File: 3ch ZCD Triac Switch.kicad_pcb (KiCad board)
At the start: 2 copper layers, 50 x 50 mm, 41 parts, among them P1 Mains_In, P2 Load_3, P3 Load_2, P4 Load_1, P5 CONN_01X06, U1 TRIAC, U2 TRIAC, U3 TRIAC, U4 TLP291, U5 TLP291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

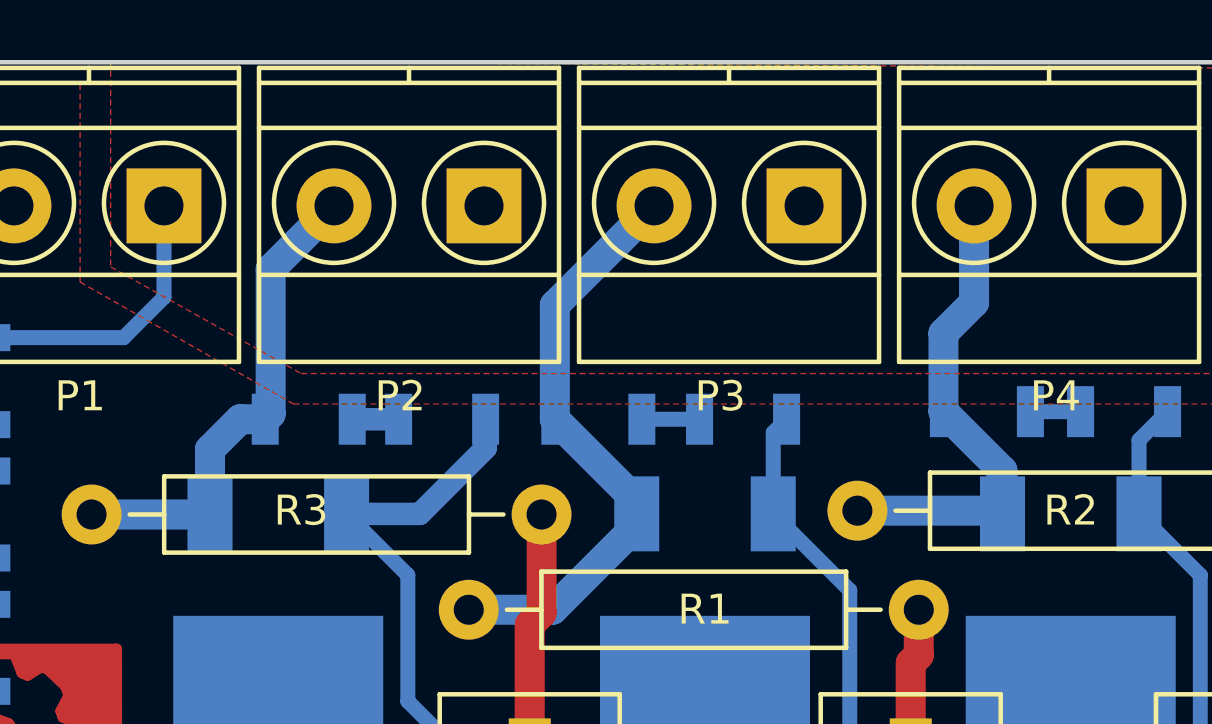
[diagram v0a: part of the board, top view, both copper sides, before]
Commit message: Triac Track Change to 2mm
2.9A with 10CdT
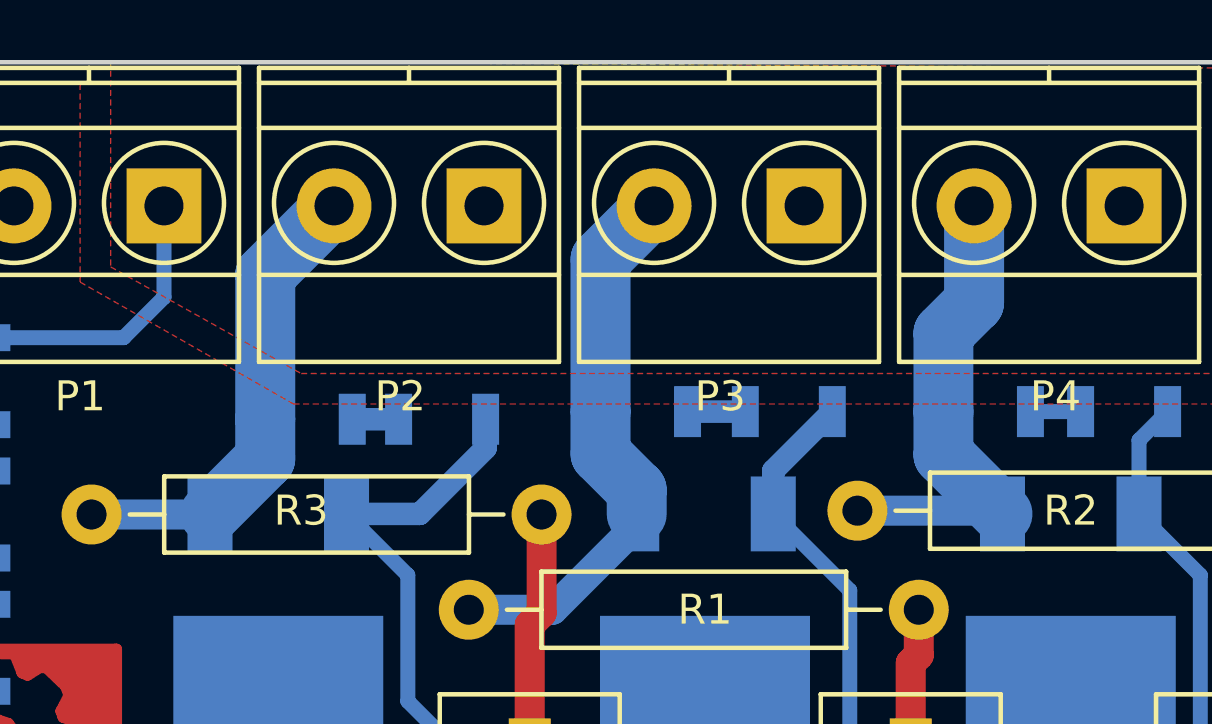
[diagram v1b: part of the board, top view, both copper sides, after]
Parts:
- moved R13 1.55 mm to (148.2, 81.6)
- moved R8 1.55 mm to (143.4, 81.6)
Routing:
- net /PH2_Out: track 20.7 -> 19.1 mm
- net /G2_Drv: track 28.3 -> 29.2 mm
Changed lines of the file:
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@@
     (links 61)
     (no_connects 0)
-    (area 116.924999 69.924999 167.075001 120.075001)
+    (area 106.479926 69.762999 167.075001 122.5)
     (thickness 1.6)
     (drawings 11)
-    (tracks 191)
+    (tracks 189)
     (zones 0)
     (modules 41)
@@
   )
   (setup
-    (last_trace_width 0.25)
+    (last_trace_width 1)
     (user_trace_width 0.25)
     (user_trace_width 0.5)
@@
     (uvia_drill 0.1)
   )
+  (module .pretty:SOT-428 (layer B.Cu)
+    (at 145.448 88.504)
+    (descr SOT428)
+    (attr smd)
+    (fp_text reference U1 (at 0 8.89 180) (layer B.SilkS)
+      (effects (font (size 1 1) (thickness 0.15)) (justify mirror))
+    )
+    (fp_text value TRIAC (at -0.09906 -0.89916) (layer B.Fab)
+      (effects (font (size 1 1) (thickness 0.15)) (justify mirror))
+    )
+    (fp_line (start -4.064 -1.016) (end 3.937 -1.016) (layer B.SilkS) (width 0.15))
+    (fp_line (start -4.064 5.588) (end -4.064 -4.445) (layer B.SilkS) (width 0.15))
+    (fp_line (start 3.937 5.588) (end 3.937 -4.445) (layer B.SilkS) (width 0.15))
+    (pad 1 smd rect (at -2.27584 -3.44932) (size 1.50114 2.49936) (layers B.Cu B.Paste B.Mask)
+      (net 7 /PH2_Out))
+    (pad 3 smd rect (at 2.27584 -3.44932) (size 1.50114 2.49936) (layers B.Cu B.Paste B.Mask)
+      (net 24 /G2_Drv))
+    (pad 2 smd rect (at 0 3.44932) (size 7.00024 7.00024) (layers B.Cu B.Paste B.Mask)
+      (net 2 /Hot_In))
+    (model TO_SOT_Packages_SMD.3dshapes/SOT-428.wrl
+      (at (xyz 0 0 0))
+      (scale (xyz 1 1 1))
+      (rotate (xyz 0 0 0))
+    )
+  )
   (module Capacitors_ThroughHole:C_Rect_L13_W6_H12_P10 (layer F.Cu)
     (at 152.306 92.568 270)
@@
   )
   (module Resistors_SMD:R_1206 (layer B.Cu)
-    (at 141.892 81.9)
+    (at 143.416 81.646)
     (descr "Resistor SMD 1206, reflow soldering, Vishay (see dcrcw.pdf)")
     (tags "resistor 1206")
@@
   )
   (module Resistors_SMD:R_1206 (layer B.Cu)
-    (at 146.718 81.9)
+    (at 148.242 81.646)
     (descr "Resistor SMD 1206, reflow soldering, Vishay (see dcrcw.pdf)")
     (tags "resistor 1206")
@@
   )
   (module .pretty:SOT-428 (layer B.Cu)
-    (at 145.448 88.504)
-    (descr SOT428)
-    (attr smd)
-    (fp_text reference U1 (at 0 8.89 180) (layer B.SilkS)
-      (effects (font (size 1 1) (thickness 0.15)) (justify mirror))
-    )
-    (fp_text value TRIAC (at -0.09906 -0.89916) (layer B.Fab)
-      (effects (font (size 1 1) (thickness 0.15)) (justify mirror))
-    )
-    (fp_line (start -4.064 -1.016) (end 3.937 -1.016) (layer B.SilkS) (width 0.15))
-    (fp_line (start -4.064 5.588) (end -4.064 -4.445) (layer B.SilkS) (width 0.15))
-    (fp_line (start 3.937 5.588) (end 3.937 -4.445) (layer B.SilkS) (width 0.15))
-    (pad 1 smd rect (at -2.27584 -3.44932) (size 1.50114 2.49936) (layers B.Cu B.Paste B.Mask)
-      (net 7 /PH2_Out))
-    (pad 3 smd rect (at 2.27584 -3.44932) (size 1.50114 2.49936) (layers B.Cu B.Paste B.Mask)
-      (net 24 /G2_Drv))
-    (pad 2 smd rect (at 0 3.44932) (size 7.00024 7.00024) (layers B.Cu B.Paste B.Mask)
-      (net 2 /Hot_In))
-    (model TO_SOT_Packages_SMD.3dshapes/SOT-428.wrl
-      (at (xyz 0 0 0))
-      (scale (xyz 1 1 1))
-      (rotate (xyz 0 0 0))
-    )
-  )
-  (module .pretty:SOT-428 (layer B.Cu)
     (at 131.224 88.504)
     (descr SOT428)
@@
   (segment (start 126.07 79.18) (end 127.414 77.836) (width 0.5) (layer B.Cu) (net 5))
   (segment (start 127.414 77.836) (end 127.414 74.788) (width 0.5) (layer B.Cu) (net 5))
-  (segment (start 128.94816 85.05468) (end 128.94816 82.90584) (width 1) (layer B.Cu) (net 6))
-  (segment (start 129.954 81.9) (end 130.79 81.9) (width 1) (layer B.Cu) (net 6))
-  (segment (start 128.94816 82.90584) (end 129.954 81.9) (width 1) (layer B.Cu) (net 6))
-  (segment (start 130.79 81.9) (end 130.97 81.72) (width 1) (layer B.Cu) (net 6))
-  (segment (start 130.97 81.72) (end 130.97 76.9) (width 1) (layer B.Cu) (net 6))
-  (segment (start 130.97 76.9) (end 133.082 74.788) (width 1) (layer B.Cu) (net 6))
+  (segment (start 130.79 81.9) (end 130.79 83.21284) (width 2) (layer B.Cu) (net 6))
+  (segment (start 130.79 83.21284) (end 128.94816 85.05468) (width 2) (layer B.Cu) (net 6))
+  (segment (start 133.082 74.788) (end 130.79 77.08) (width 2) (layer B.Cu) (net 6))
+  (segment (start 130.79 77.08) (end 130.79 81.9) (width 2) (layer B.Cu) (net 6))
   (segment (start 125.001 85.075) (end 128.92784 85.075) (width 1) (layer B.Cu) (net 6))
   (segment (start 128.92784 85.075) (end 129.05484 84.948) (width 1) (layer B.Cu) (net 6))
-  (segment (start 140.442 81.9) (end 140.442 78.096) (width 1) (layer B.Cu) (net 7))
-  (segment (start 140.442 78.096) (end 143.75 74.788) (width 1) (layer B.Cu) (net 7))
-  (segment (start 143.17216 85.05468) (end 143.17216 84.63016) (width 1) (layer B.Cu) (net 7))
-  (segment (start 143.17216 84.63016) (end 140.442 81.9) (width 1) (layer B.Cu) (net 7))
+  (segment (start 141.966 81.646) (end 141.966 76.572) (width 2) (layer B.Cu) (net 7))
+  (segment (start 141.966 76.572) (end 143.75 74.788) (width 2) (layer B.Cu) (net 7))
+  (segment (start 143.17216 84.25966) (end 141.966 83.0535) (width 2) (layer B.Cu) (net 7))
+  (segment (start 141.966 83.0535) (end 141.966 81.646) (width 2) (layer B.Cu) (net 7))
+  (segment (start 143.17216 85.05468) (end 143.17216 84.25966) (width 2) (layer B.Cu) (net 7))
+  (segment (start 143.17216 85.05468) (end 143.17216 84.63016) (width 1.8) (layer B.Cu) (net 7))
   (segment (start 143.17216 85.05468) (end 143.17216 85.44584) (width 1) (layer B.Cu) (net 7))
   (segment (start 143.17216 85.44584) (end 140.368 88.25) (width 1) (layer B.Cu) (net 7))
   (segment (start 140.368 88.25) (end 137.574 88.25) (width 1) (layer B.Cu) (net 7))
-  (segment (start 140.442 81.9) (end 140.442 82.32452) (width 0.75) (layer B.Cu) (net 7))
-  (segment (start 140.442 81.9) (end 140.442 81.572) (width 0.5) (layer B.Cu) (net 7))
-  (segment (start 155.36416 85.05468) (end 155.36416 83.61416) (width 1) (layer B.Cu) (net 8))
-  (segment (start 155.36416 83.61416) (end 153.396 81.646) (width 1) (layer B.Cu) (net 8))
+  (segment (start 153.396 81.646) (end 153.396 83.08652) (width 2) (layer B.Cu) (net 8))
+  (segment (start 153.396 83.08652) (end 155.36416 85.05468) (width 2) (layer B.Cu) (net 8))
+  (segment (start 153.396 79.032) (end 153.396 81.646) (width 2) (layer B.Cu) (net 8))
+  (segment (start 154.418 74.788) (end 154.418 78.01) (width 2) (layer B.Cu) (net 8))
+  (segment (start 154.418 78.01) (end 153.396 79.032) (width 2) (layer B.Cu) (net 8))
   (segment (start 150.528 84.948) (end 155.25748 84.948) (width 1) (layer B.Cu) (net 8))
   (segment (start 155.25748 84.948) (end 155.36416 85.05468) (width 1) (layer B.Cu) (net 8))
-  (segment (start 153.396 81.646) (end 153.396 79.032) (width 1) (layer B.Cu) (net 8))
-  (segment (start 153.396 79.032) (end 154.418 78.01) (width 1) (layer B.Cu) (net 8))
-  (segment (start 154.418 78.01) (end 154.418 74.788) (width 1) (layer B.Cu) (net 8))
   (segment (start 158.656 114.158) (end 156.37 114.158) (width 0.5) (layer B.Cu) (net 9))
   (segment (start 132.24 117.968) (end 132.24 116.19) (width 0.5) (layer B.Cu) (net 9))
@@
   (segment (start 121.445 86.525) (end 121.445 88.07) (width 0.5) (layer B.Cu) (net 17))
   (segment (start 118.905 86.525) (end 118.905 88.07) (width 0.5) (layer B.Cu) (net 18))
-  (segment (start 143.342 81.9) (end 145.268 81.9) (width 0.5) (layer B.Cu) (net 19))
+  (segment (start 146.792 81.646) (end 144.866 81.646) (width 0.75) (layer B.Cu) (net 19))
   (segment (start 133.69 81.9) (end 135.235 81.9) (width 0.75) (layer B.Cu) (net 20))
   (segment (start 156.296 81.646) (end 157.968 81.646) (width 0.5) (layer B.Cu) (net 21))
   (segment (start 121.445 90.97) (end 121.445 92.515) (width 0.5) (layer B.Cu) (net 22))
   (segment (start 118.905 90.97) (end 118.905 92.515) (width 0.5) (layer B.Cu) (net 23))
+  (segment (start 147.72384 85.05468) (end 147.72384 83.61416) (width 0.75) (layer B.Cu) (net 24))
+  (segment (start 147.72384 83.61416) (end 149.692 81.646) (width 0.75) (layer B.Cu) (net 24))
   (segment (start 152.687 106.411) (end 152.687 105.649) (width 0.5) (layer B.Cu) (net 24))
   (segment (start 152.687 105.649) (end 154.592 103.744) (width 0.5) (layer B.Cu) (net 24))
@@
   (segment (start 150.274 94.346) (end 150.274 87.60484) (width 0.5) (layer B.Cu) (net 24))
   (segment (start 150.274 87.60484) (end 147.72384 85.05468) (width 0.5) (layer B.Cu) (net 24))
-  (segment (start 147.72384 85.05468) (end 147.72384 82.34416) (width 0.5) (layer B.Cu) (net 24))
-  (segment (start 147.72384 82.34416) (end 148.168 81.9) (width 0.5) (layer B.Cu) (net 24))
   (segment (start 163.736 106.538) (end 163.736 105.776) (width 0.5) (layer B.Cu) (net 25))
   (segment (start 163.736 105.776) (end 165.26 104.252) (width 0.5) (layer B.Cu) (net 25))
